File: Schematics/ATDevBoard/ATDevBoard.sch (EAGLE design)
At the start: 39 parts, among them U1 TINY85-20-DIP

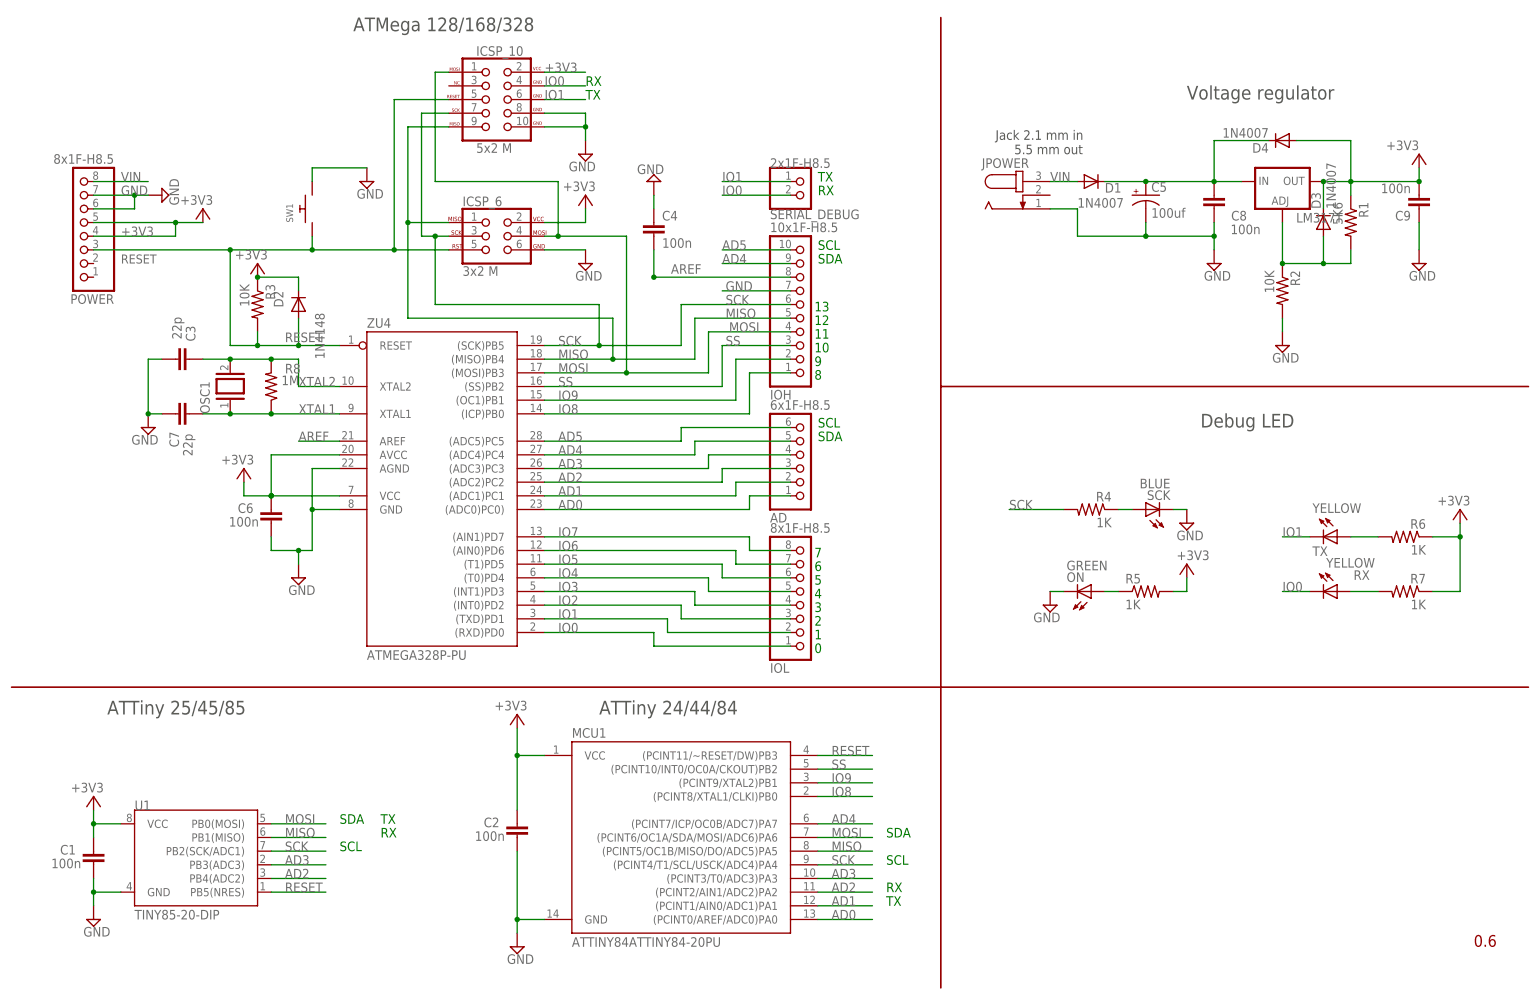
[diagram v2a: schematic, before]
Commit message: Fixed some components package with buy info, revisited board layout.
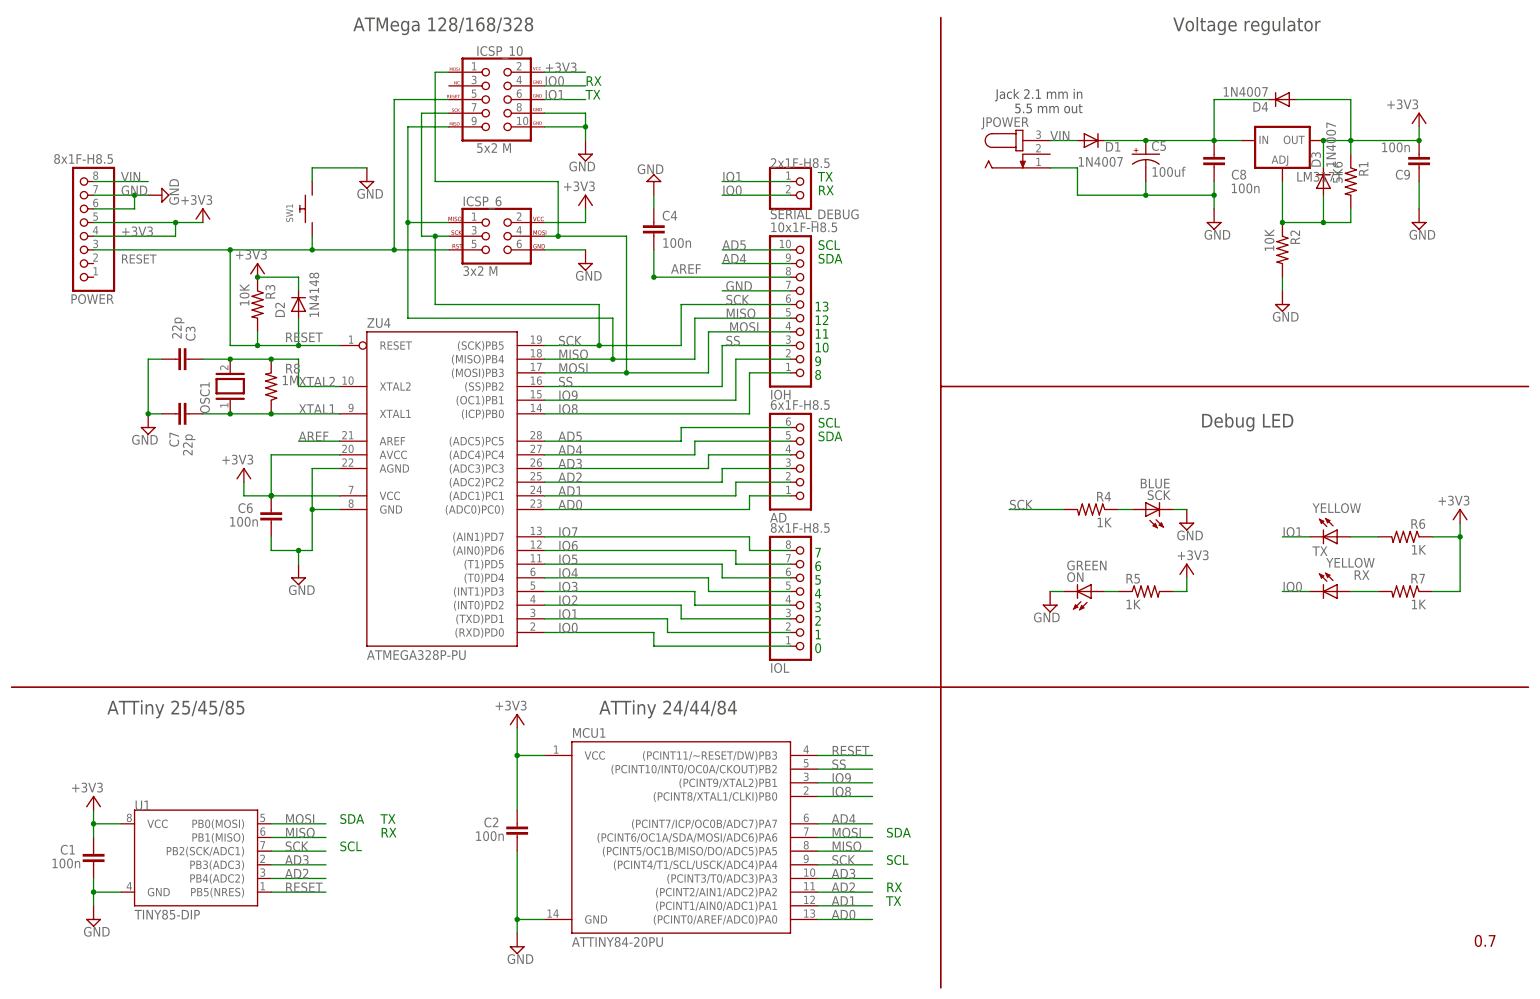
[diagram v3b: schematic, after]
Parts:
- C3, C7: device SmartPrj:C-EU025-024X044 -> SmartPrj:C-EU050-024X044
- D2: device diode:1N4148DO35-10 -> adafruit:DIODESOD-323F
- MCU1: value ATTINY84ATTINY84-20PU -> ATTINY84-20PU
- R8: device rcl:R-US_0309/12 -> rcl:R-US_0207/10
- U1: value TINY85-20-DIP -> TINY85-DIP
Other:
- moved on the sheet: C5, C8, C9, D1, D3, D4, JPOWER, LM317T, R1, R2

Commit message: Added micro USB, trimmer and PTC fuse
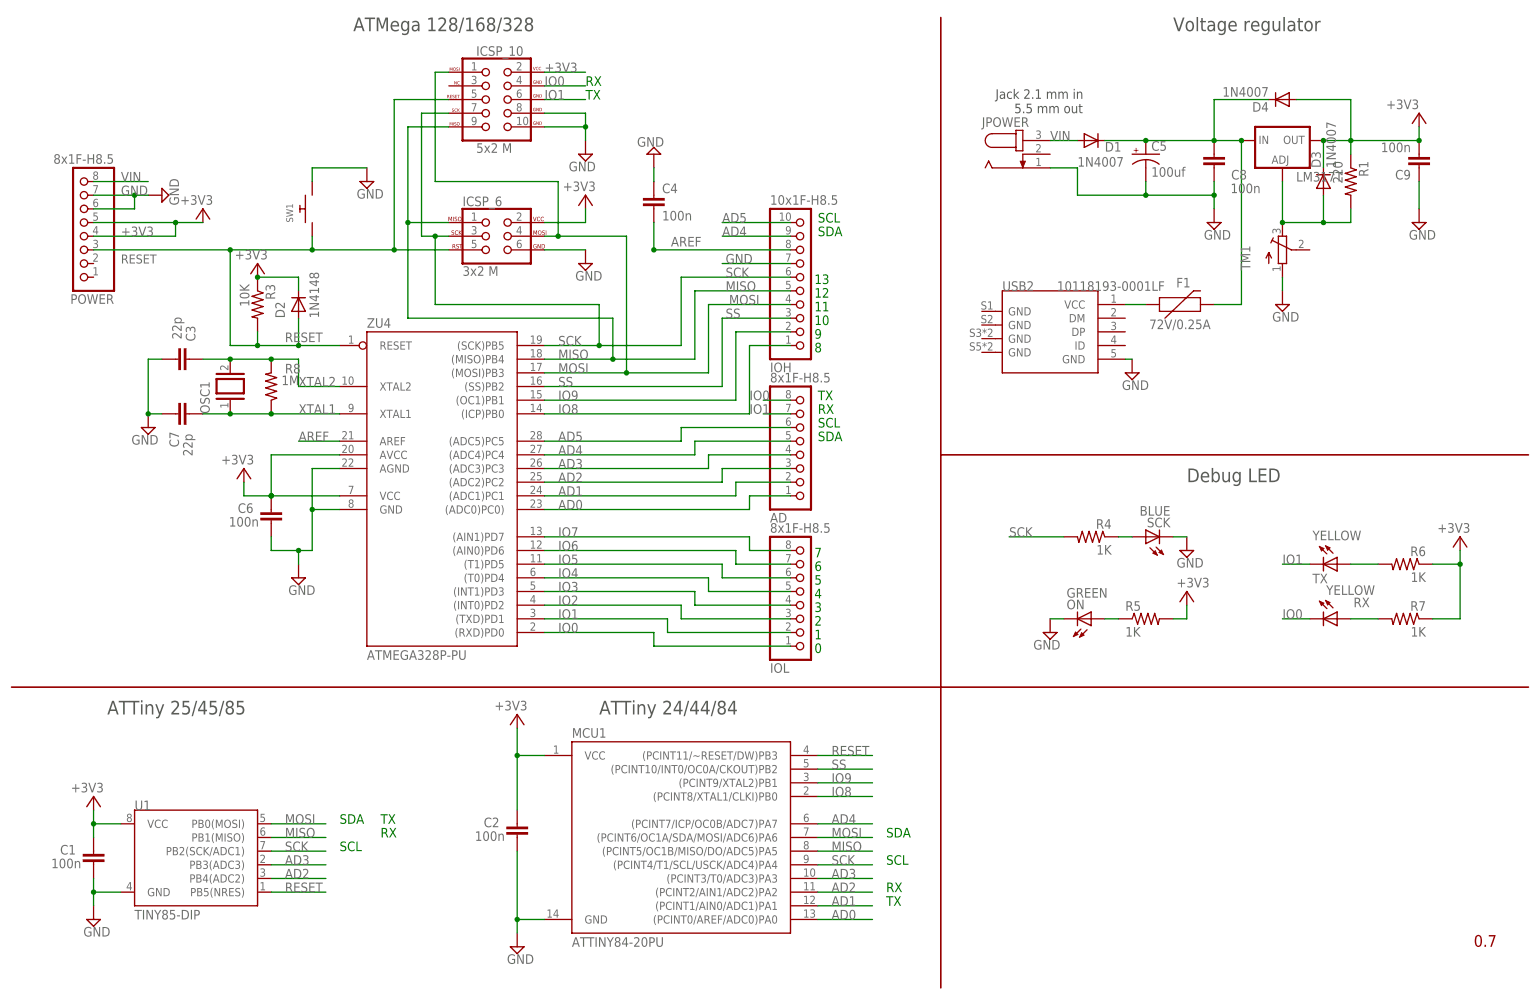
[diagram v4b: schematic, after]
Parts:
- removed R2: 10K, rcl:R-US_0309/12
- removed SERIAL_DEBUG: 2x1F-H8.5, pinhead:PINHD-1X2
- added F1: 72V/0.25A, SparkFun-Fuses:PPTC_PTH
- added TM1: (no value), adafruit:TRIMPOT3386
- added USB2: 10118193-0001LF, Seeed-OPL-Connector:MICRO-USB-SMD-B-(10118193-0001LF)
- AD: value 6x1F-H8.5 -> 8x1F-H8.5; device pinhead:PINHD-1X6 -> pinhead:PINHD-1X8
- LM317T: device v-reg:LM317TL -> v-reg:LM317TS
- R1: value 5K6 -> 220; device rcl:R-US_0309/12 -> rcl:R-US_0204/7
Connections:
- new net N$5: F1.1, USB2.VCC
- net GND: now also TM1.A, USB2.GND@5; no longer R2.2
- net IO0: now also AD.8; no longer SERIAL_DEBUG.2
- net IO1: now also AD.7; no longer SERIAL_DEBUG.1
- net N$1: now also TM1.E; no longer R2.1
- net N$2: now also F1.2
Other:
- moved on the sheet: C4, IOH, ON, R4, R5, R6, R7, RX, SCK, TX

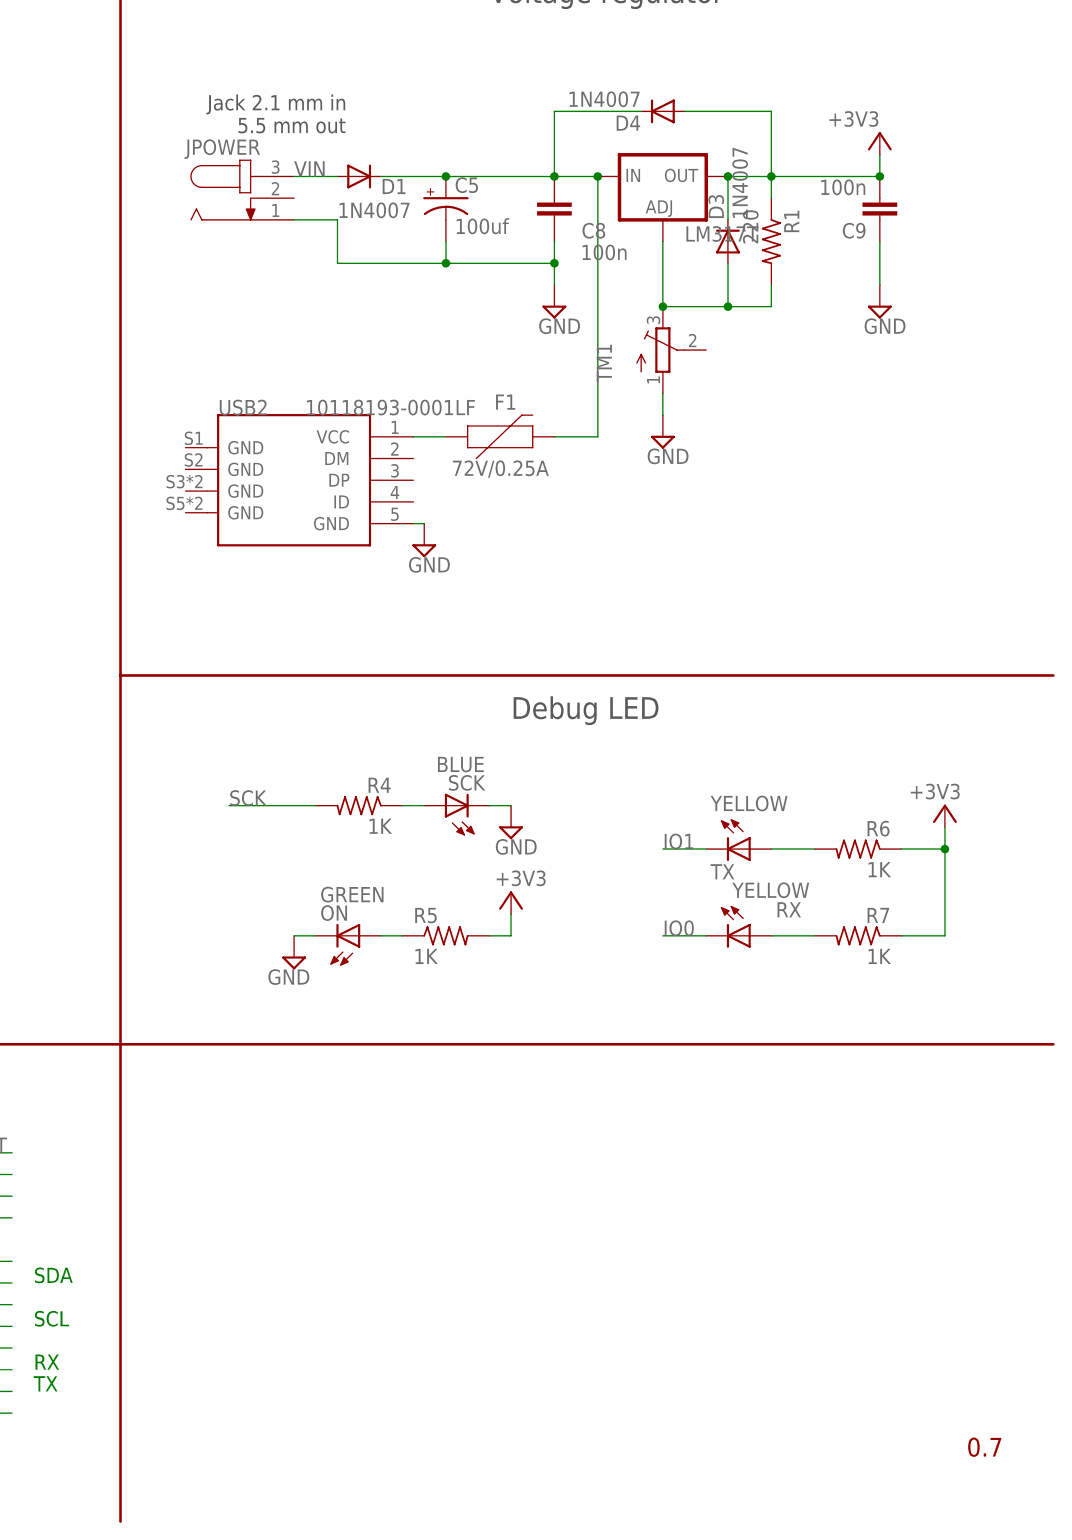
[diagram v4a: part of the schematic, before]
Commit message: Added plated slot for DC plug, new device for micro USB connector, updated partlist
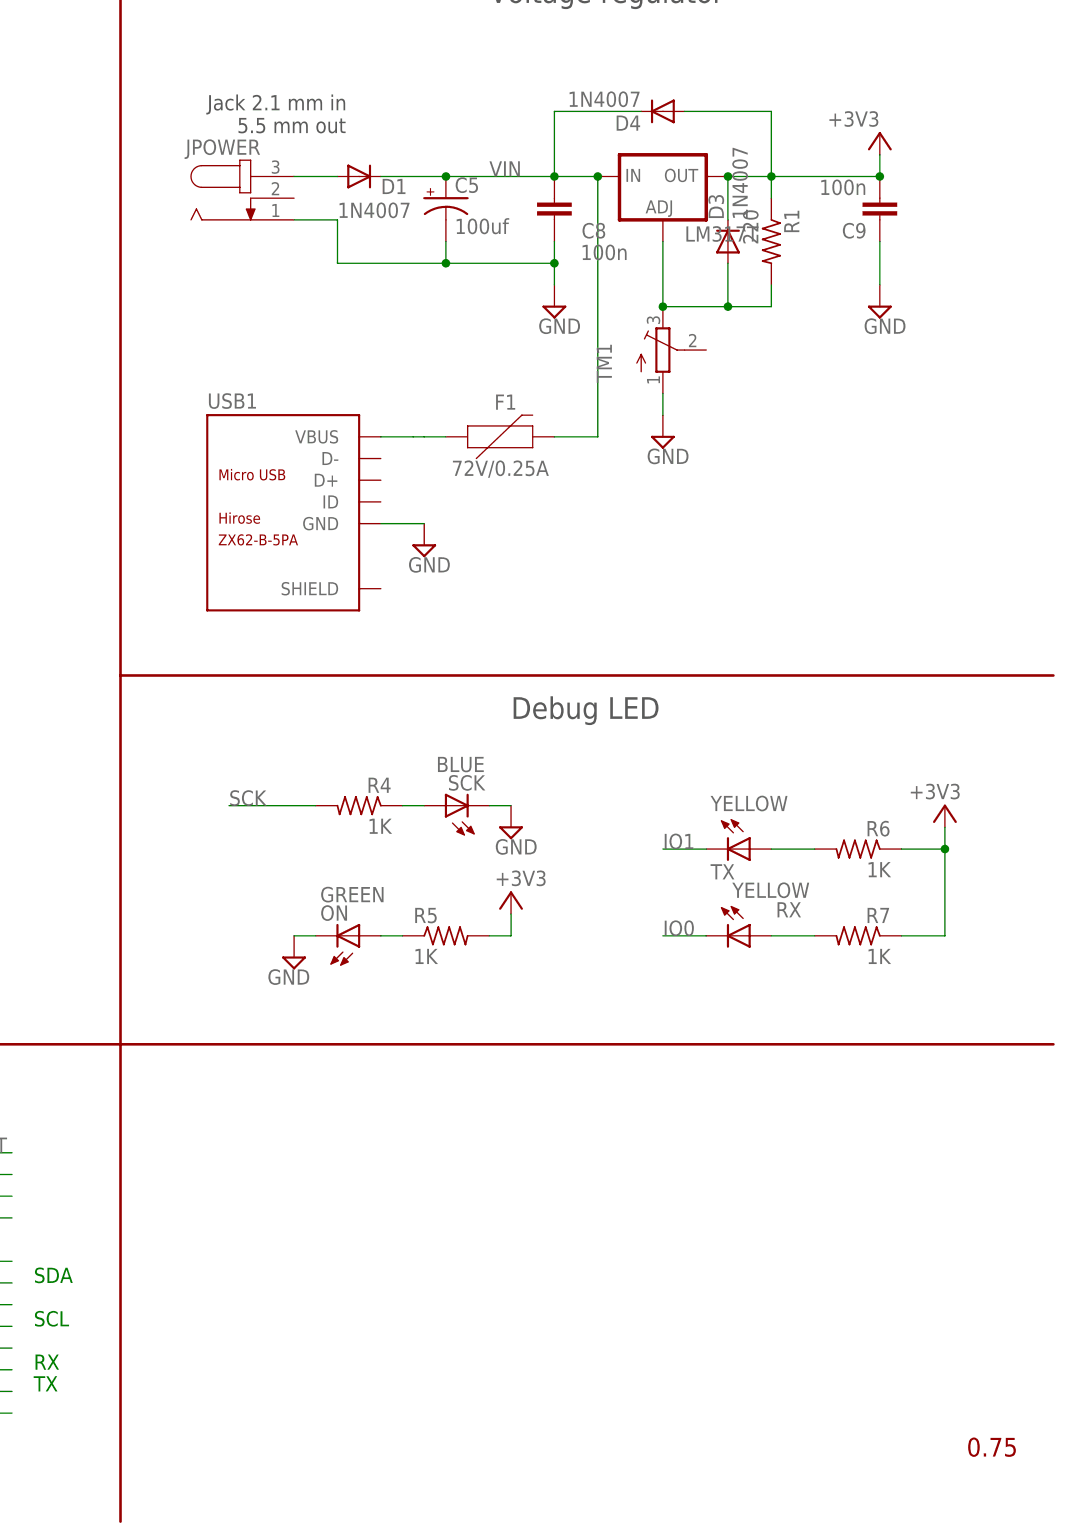
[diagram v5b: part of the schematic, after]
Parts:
- removed USB2: 10118193-0001LF, Seeed-OPL-Connector:MICRO-USB-SMD-B-(10118193-0001LF)
- added USB1: ZX62-B-5PA, Seeed-Connector:MICRO-USB-SMD(ZX62-B-5PA)
- JPOWER: device con-jack:JACK-PLUG0 -> con-jack-plated-slots:JACK-PLUG0
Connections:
- removed net N$5: F1.1, USB2.VCC
- new net VBUS: F1.1, USB1.VBUS
- net GND: now also USB1.GND; no longer USB2.GND@5
- net N$2: now also D1.A, JPOWER.3; no longer C5.+, C8.2, D1.C, D4.C, F1.2, LM317T.IN
- net VIN: now also C5.+, C8.2, D1.C, D4.C, F1.2, LM317T.IN; no longer D1.A, JPOWER.3
